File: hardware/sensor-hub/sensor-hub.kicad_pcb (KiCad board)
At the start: 4 copper layers, 96 x 81 mm, 117 parts, among them J1 Conn_ARM_JTAG_SWD_10, J10 BATT, J2 Micro_SD_Card_Det2, J3 RJ45_Wuerth_7499010121A, J4 PWR, J5 LCD_CONN, J6 ENC_CONN, J7 RADIO_CONN, J8 UART_CONN, J9 I2C_CONN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

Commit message: Restart layout with proper constraints
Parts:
- TP2: moved to B.Cu
- moved C28 86.4 mm to (140.4, 43.1)
- moved JP5 67.2 mm to (159.2, 43.8)
- moved C35 67.2 mm to (157.9, 52.9), turned to 180 degrees
- moved C34 61.3 mm to (174.9, 49.2), turned to 90 degrees
- moved U5 50.6 mm to (170.0, 61.7)
- moved U8 49.6 mm to (171.0, 49.6)
- moved U7 48.4 mm to (158.2, 48.9)
- moved C33 42.1 mm to (167.9, 71.3), turned to 180 degrees
- moved D3 38.0 mm to (18.1, 166.4), turned to 180 degrees
- moved R37 35.2 mm to (136.2, 103.5), turned to -90 degrees
- moved R32 31.1 mm to (134.8, 103.5), turned to 90 degrees
- moved R31 30.9 mm to (131.8, 103.5), turned to 90 degrees
- moved C24 30.0 mm to (32.4, 157.8), turned to -90 degrees
- moved FB1 29.1 mm to (130.7, 90.1), turned to -90 degrees
- moved R14 28.8 mm to (19.0, 170.8), turned to 180 degrees
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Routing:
- net /W5500/ACT_LED: track 0.00 -> 39.1 mm, vias 0 -> 2
- net /W5500/LINK_LED: track 0.00 -> 34.3 mm, vias 0 -> 2
- net Net-(J3-Pad12): track 0.00 -> 26.5 mm, vias 0 -> 1
- net Net-(J3-Pad11): track 0.00 -> 23.9 mm, vias 0 -> 1
- net Net-(J3-Pad10): track 0.00 -> 20.2 mm, vias 0 -> 1
- net Net-(J3-Pad9): track 0.00 -> 19.3 mm, vias 0 -> 1
- net Net-(U1-PH1): track 3.37 -> 14.0 mm
- net Net-(JP3-C): track 0.00 -> 8.20 mm
- net Net-(JP1-C): track 0.00 -> 7.82 mm
- net Net-(U1-PH0): track 3.34 -> 10.4 mm
- net +3.3V: track 8.46 -> 15.5 mm, vias 0 -> 2
- net /W5500/ETH_TXP: track 37.7 -> 31.6 mm, vias 2 -> 0
- net Net-(JP2-C): track 0.00 -> 6.05 mm
- net /W5500/ETH_TXN: track 37.2 -> 31.6 mm, vias 2 -> 0
- net Net-(U1-PC15): track 3.30 -> 8.54 mm
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- added copper zone on In1.Cu, net GND

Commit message: Core layout done
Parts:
- C22: moved to B.Cu
- moved J10 196.4 mm to (62.2, 74.8)
- moved C22 177.0 mm to (96.8, 86.0)
- moved J5 164.0 mm to (110.3, 68.2), turned to -90 degrees
- moved R23 150.4 mm to (80.8, 97.4)
- moved J7 149.2 mm to (127.0, 68.0), turned to -90 degrees
- moved D1 147.4 mm to (81.4, 101.4)
- moved J6 145.5 mm to (57.7, 101.8), turned to 180 degrees
- moved R27 144.9 mm to (63.2, 95.7), turned to 90 degrees
- moved R24 143.2 mm to (67.8, 95.7), turned to 90 degrees
- moved R25 142.9 mm to (66.3, 95.7), turned to 90 degrees
- moved R21 140.6 mm to (80.8, 93.8)
- moved R22 140.0 mm to (80.9, 95.7)
- moved C26 139.9 mm to (93.3, 180.0)
- moved R15 139.9 mm to (86.0, 172.0)
- moved R16 139.9 mm to (86.0, 175.0)
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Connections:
- net Net-(D3-A) renamed /Power/3.3V_P0
- net Net-(U3-LX) renamed /Power/LX
- J2 pad 1: /MCU/SDIO_DAT2 -> /MCU/SDIO_DAT1
- J2 pad 2: /MCU/SDIO_DAT3 -> /MCU/SDIO_DAT0
- J2 pad 3: /MCU/SDIO_CMD -> GND
- J2 pad 4: +3.3V -> /MCU/SDIO_CK
- J2 pad 5: /MCU/SDIO_CK -> +3.3V
- J2 pad 6: GND -> /MCU/SDIO_CMD
- J2 pad 7: /MCU/SDIO_DAT0 -> /MCU/SDIO_DAT3
- J2 pad 8: /MCU/SDIO_DAT1 -> /MCU/SDIO_DAT2
- J2 pad SH: (no net) -> GND
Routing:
- net /SYS_RESET: track 0.00 -> 57.6 mm, vias 0 -> 3
- net GND: track 46.9 -> 92.0 mm, vias 41 -> 80
- net /MCU/CARD_DET: track 0.00 -> 40.8 mm, vias 0 -> 2
- net +BATT: track 1.61 -> 41.6 mm
- net /MCU/SDIO_DAT0: track 0.00 -> 39.0 mm, vias 0 -> 1
- net /MCU/SDIO_DAT1: track 0.00 -> 38.9 mm
- net /MCU/SDIO_DAT2: track 0.00 -> 38.7 mm
- net /MCU/SDIO_CK: track 0.00 -> 36.4 mm
- net /MCU/SDIO_DAT3: track 0.00 -> 33.2 mm, vias 0 -> 1
- net /MCU/ETH_INT: track 1.68 -> 34.2 mm, vias 0 -> 2
- net /MCU/ETH_CS: track 4.39 -> 33.6 mm, vias 0 -> 2
- net /MCU/ETH_SCK: track 3.69 -> 31.5 mm, vias 0 -> 2
- net /LCD_MOSI: track 0.00 -> 25.5 mm, vias 0 -> 1
- net /LCD_BL_PWM: track 0.00 -> 25.3 mm, vias 0 -> 1
- net /MCU/SDIO_CMD: track 0.00 -> 22.9 mm
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- added copper zone on In2.Cu, net +3.3V
- added copper zone on In2.Cu, net +3.3VA
- added copper zone on F.Cu, net /Power/3.3V_P0
- added copper zone on F.Cu, net /Power/LX
- added copper zone on F.Cu, net Earth
- added copper zone on F.Cu, net VBUS
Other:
- board text removed: "holes: 86x51"

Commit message: Most layout done
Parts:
- added TP1: TestPoint, TestPoint:TestPoint_Pad_D1.0mm, F.Cu at (62.8, 126.9)
- C22: moved to F.Cu
- C26, C27, JP4, JP5: moved to B.Cu
- moved J9 138.0 mm to (62.5, 101.7), turned to 90 degrees
- moved C34 123.9 mm to (61.1, 98.3), turned to 180 degrees
- moved C27 121.1 mm to (88.7, 123.9), turned to 180 degrees
- moved JP5 120.8 mm to (54.7, 104.2), turned to 180 degrees
- moved U8 119.1 mm to (61.2, 95.8)
- moved U5 118.1 mm to (54.6, 86.9), turned to 90 degrees
- moved U7 116.4 mm to (54.1, 101.0)
- moved R33 115.2 mm to (75.0, 97.3), turned to 90 degrees
- moved C35 113.2 mm to (54.0, 97.8), turned to 0 degrees
- moved R34 113.2 mm to (76.5, 97.3), turned to 90 degrees
- moved C33 107.5 mm to (61.8, 88.8), turned to -90 degrees
- moved C28 87.0 mm to (75.0, 100.6), turned to 90 degrees
- moved R28 63.6 mm to (98.5, 119.9), turned to 180 degrees
- moved SW1 63.2 mm to (84.3, 101.4), turned to 90 degrees
- moved R17 60.8 mm to (90.3, 118.9)
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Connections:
- R21 pad 1: Net-(U4-P4) -> Net-(U4-P5)
- R22 pad 1: Net-(U4-P5) -> Net-(U4-P6)
- R23 pad 1: Net-(U4-P6) -> Net-(U4-P7)
- U4 pad 10: /MCU/CARD_DET -> Net-(U4-P7)
- U4 pad 7: Net-(U4-P4) -> /MCU/CARD_DET
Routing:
- net /MCU/SCL: track 1.07 -> 61.5 mm, vias 1 -> 2
- net /MCU/SDA: track 1.45 -> 59.0 mm, vias 1 -> 4
- net +3.3V: track 26.1 -> 76.6 mm, vias 11 -> 33
- net /ENC_BTN: track 0.00 -> 46.0 mm, vias 0 -> 2
- net /ENC_B: track 0.00 -> 44.3 mm, vias 0 -> 2
- net /MCU/RADIO_CE: track 3.11 -> 45.9 mm, vias 0 -> 2
- net /ENC_A: track 0.00 -> 42.3 mm, vias 0 -> 2
- net /SYS_RESET: track 57.6 -> 98.7 mm, vias 3 -> 6
- net /MCU/GPIO3: track 0.00 -> 40.3 mm, vias 0 -> 3
- net /MCU/SWDIO: track 0.95 -> 40.0 mm, vias 1 -> 6
- net /MCU/SWCLK: track 0.86 -> 39.3 mm, vias 1 -> 4
- net /MCU/RADIO_MOSI: track 2.46 -> 35.7 mm, vias 0 -> 2
- net GND: track 92.0 -> 121.3 mm, vias 80 -> 105
- net /MCU/USART2_RX: track 0.00 -> 21.3 mm
- net /MCU/SDIO_CMD: track 22.9 -> 43.9 mm, vias 0 -> 2
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- added copper zone on F.Cu, net +3.3V
- added copper zone on B.Cu, net GND

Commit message: Layout
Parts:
- moved C34 35.8 mm to (49.1, 64.6), turned to 90 degrees
- moved U8 32.5 mm to (51.8, 64.6), turned to -90 degrees
- moved JP5 23.4 mm to (60.0, 81.4), turned to -90 degrees
- moved U7 19.2 mm to (56.8, 81.9), turned to 90 degrees
- moved C35 13.7 mm to (57.1, 84.5)
- moved U5 5.70 mm to (57.1, 92.0)
- moved C33 5.65 mm to (64.3, 93.9)
- moved J10 2.72 mm to (70.4, 84.1)
- moved TP2 2.09 mm to (85.6, 81.0)
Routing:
- net GND: track 121.3 -> 172.8 mm, vias 105 -> 281
- net /MCU/SCL: track 61.5 -> 112.2 mm
- net /MCU/SDA: track 59.0 -> 103.0 mm, vias 4 -> 7
- net +3.3V: track 76.6 -> 101.7 mm, vias 33 -> 40
- net /MCU/ETH_MOSI: track 23.1 -> 39.2 mm
- net /MCU/ETH_MISO: track 23.8 -> 39.5 mm
- net /LCD_MOSI: track 27.7 -> 23.4 mm
- net /MCU/NRST: track 13.5 -> 16.6 mm
- net Net-(JP5-C): track 0.00 -> 2.46 mm, vias 0 -> 1
- net /MCU/RADIO_MOSI: track 35.7 -> 38.0 mm
- net Net-(U1-PC13): track 9.58 -> 11.6 mm
- net /MCU/ETH_INT: track 41.1 -> 39.3 mm
- net unconnected-(J1-KEY-Pad7): track 1.60 -> 0.00 mm, vias 1 -> 0
- net /MCU/SWDIO: track 40.0 -> 41.6 mm
- net /MCU/SWCLK: track 39.3 -> 40.5 mm
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
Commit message: DRC fixes
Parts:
- D1: value LED_BGKR -> LED_BGRA
- moved JP4 1.62 mm to (75.6, 99.8), turned to 90 degrees
- turned D1 to 0 degrees
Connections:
- D1 pad 1: Net-(D1-BA) -> Net-(D1-BK)
- D1 pad 3: GND -> Net-(D1-RK)
- D1 pad 4: Net-(D1-RA) -> +3.3V
- R21 pad 2: Net-(D1-BA) -> Net-(D1-RK)
- R23 pad 2: Net-(D1-RA) -> Net-(D1-BK)
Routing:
- net Net-(D1-BK): track 0.00 -> 4.41 mm
- net Net-(JP4-C): track 2.69 -> 5.60 mm
- net +3.3V: track 101.7 -> 104.5 mm, vias 40 -> 42
- net Net-(D1-RA): track 2.59 -> 0.00 mm
- net Net-(D1-BA): track 2.59 -> 0.00 mm
- net Net-(D1-RK): track 0.00 -> 2.58 mm
- net Net-(D1-GK): track 4.57 -> 2.98 mm
- net /MCU/SDIO_CK: track 43.1 -> 44.2 mm
- net +3.3VA: track 19.5 -> 20.7 mm, vias 10 -> 11
- net /MCU/SDIO_CMD: track 42.9 -> 43.8 mm
- net GND: track 172.8 -> 173.4 mm, vias 281 -> 285

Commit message: Finalize layout
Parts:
- added C44: 10u, Capacitor_SMD:C_0805_2012Metric, B.Cu at (49.6, 113.8)
- added C45: 22u, Capacitor_SMD:C_0805_2012Metric, B.Cu at (56.5, 101.6)
- added C46: 22u, Capacitor_SMD:C_0805_2012Metric, B.Cu at (56.5, 99.5)
- added D4: LED, LED_SMD:LED_0603_1608Metric, F.Cu at (50.6, 100.8)
- added R38: 1k, Resistor_SMD:R_0603_1608Metric, F.Cu at (49.0, 100.8)
- added REF**: KiCad-Logo2_5mm_SilkScreen, Symbol:KiCad-Logo2_5mm_SilkScreen, F.Cu at (128.2, 65.6)
- added REF**: OSHW-Symbol_6.7x6mm_SilkScreen, Symbol:OSHW-Symbol_6.7x6mm_SilkScreen, F.Cu at (134.4, 134.4)
- added U6: AMS1117-3.3, Package_TO_SOT_SMD:SOT-223-3_TabPin2, B.Cu at (53.0, 108.2)
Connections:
- C33 pad 1: +3.3V -> +3.3V_LDO
- C34 pad 1: +3.3V -> +3.3V_LDO
- C35 pad 1: +3.3V -> +3.3V_LDO
- JP5 pad 3: +3.3V -> +3.3V_LDO
- U5 pad 19: +3.3V -> +3.3V_LDO
- U5 pad 7: +3.3V -> +3.3V_LDO
- U7 pad 1: +3.3V -> +3.3V_LDO
- U7 pad 10: +3.3V -> +3.3V_LDO
- U7 pad 6: +3.3V -> +3.3V_LDO
- U8 pad 1: /MCU/SCL -> /MCU/SDA
- U8 pad 5: +3.3V -> +3.3V_LDO
- U8 pad 6: /MCU/SDA -> /MCU/SCL
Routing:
- net +3.3V_LDO: track 0.00 -> 28.1 mm, vias 0 -> 13
- net +3.3V: track 104.5 -> 79.1 mm, vias 42 -> 33
- net /MCU/SDA: track 103.0 -> 107.7 mm, vias 7 -> 8
- net /MCU/SCL: track 112.2 -> 108.7 mm
- net /MCU/ETH_MISO: track 39.5 -> 41.4 mm
- net Net-(D4-K): track 0.00 -> 1.67 mm
- net /MCU/GPIO3: track 40.7 -> 42.0 mm
- net /MCU/ETH_MOSI: track 39.2 -> 40.3 mm
- net GND: track 173.4 -> 174.1 mm, vias 285 -> 320
- net /ENC_A: track 42.3 -> 42.5 mm, vias 2 -> 3
- net /ENC_B: track 44.3 -> 44.4 mm, vias 2 -> 3
- net VBUS: vias 2 -> 5
- added copper zone on B.Cu, net +3.3V_LDO
- added copper zone on In2.Cu, net +3.3V_LDO
- added copper zone on B.Cu, net VBUS
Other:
- board text added: "+5V"
- board text added: "3V3"
- board text added: "GND"
- board text added: "Licensed under CERN-OHL-P v2 or later"
- board text added: "RX<"
- board text added: "SCL"
- board text added: "SDA"
- board text added: "TX>"
- board text added: "github.com/Aifryz/sensor-hub"
- board text added: "sensor-hub v1.0"

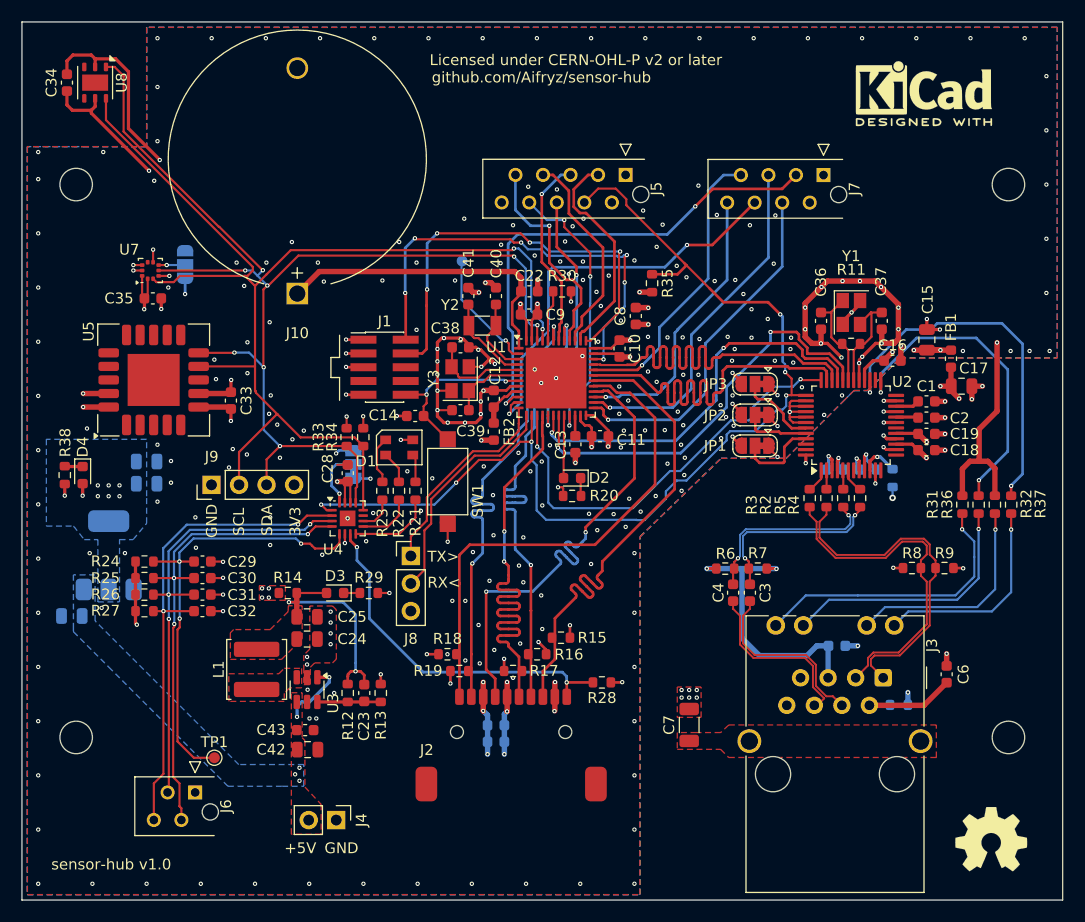
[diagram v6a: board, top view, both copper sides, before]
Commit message: V1.0
Fixed value typos, replaced vias with 0.3/0.45, added production files
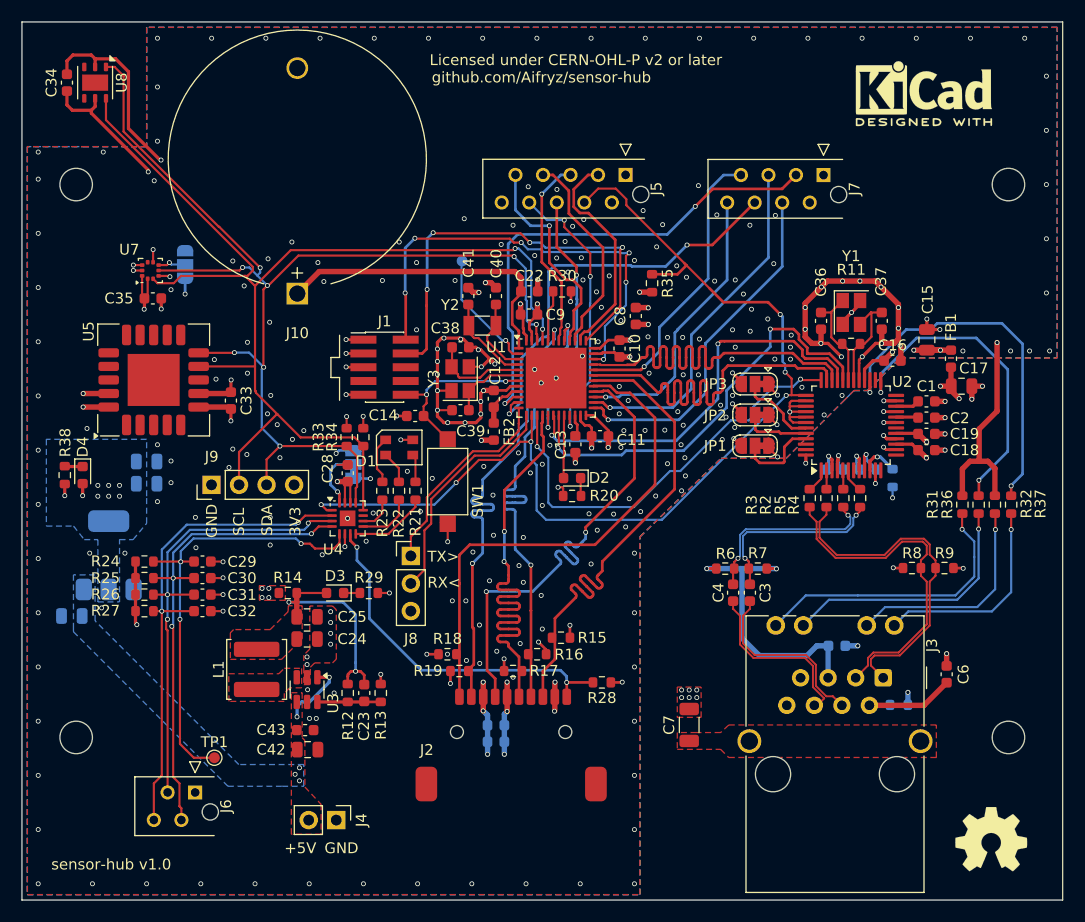
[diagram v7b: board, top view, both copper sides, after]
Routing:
- net /SYS_RESET: track 98.7 -> 97.4 mm
- net +3.3VA: track 20.8 -> 21.7 mm
- net /MCU/ETH_SCK: track 37.0 -> 37.7 mm
- net GND: track 174.1 -> 174.8 mm, vias 320 -> 318
- net /MCU/SWCLK: track 40.5 -> 41.2 mm
- net Net-(U4-P5): track 7.78 -> 7.21 mm
- net /MCU/ETH_CS: track 39.0 -> 39.5 mm
